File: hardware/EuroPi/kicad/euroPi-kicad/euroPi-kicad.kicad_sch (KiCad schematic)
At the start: 108 parts, among them J1 Output 1 Jack, J10 Eurorack Power 2x8 16p, J11 Conn_01x13_Socket, J12 OLED 64x128, J13 USB_B_Micro, J14 Conn_01x03_Pin, J16 Conn_02x04_Top_Bottom, J17 Conn_01x13_Pin, J18 Conn_01x04_Pin, J19 Conn_01x04_Socket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

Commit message: cleaning pcb fixing connector i2c
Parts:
- added J15: Conn_01x04_Pin, Connector_PinSocket_2.54mm:PinSocket_1x04_P2.54mm_Vertical, symbol Connector:Conn_01x04_Pin
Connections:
- net +3.3V: now also J15.2 (Pin_2)
- net CPC_SCL: now also J15.3 (Pin_3); no longer J16.1 (Pin_1), U?.2 (GP1)
- net CPC_SDA: now also J15.4 (Pin_4); no longer J16.6 (Pin_6), U?.1 (GP0)
- net GND: now also J15.1 (Pin_1)
- new net GP0: J16.6 (Pin_6), U?.1 (GP0)
- new net GP1: J16.1 (Pin_1), U?.2 (GP1)

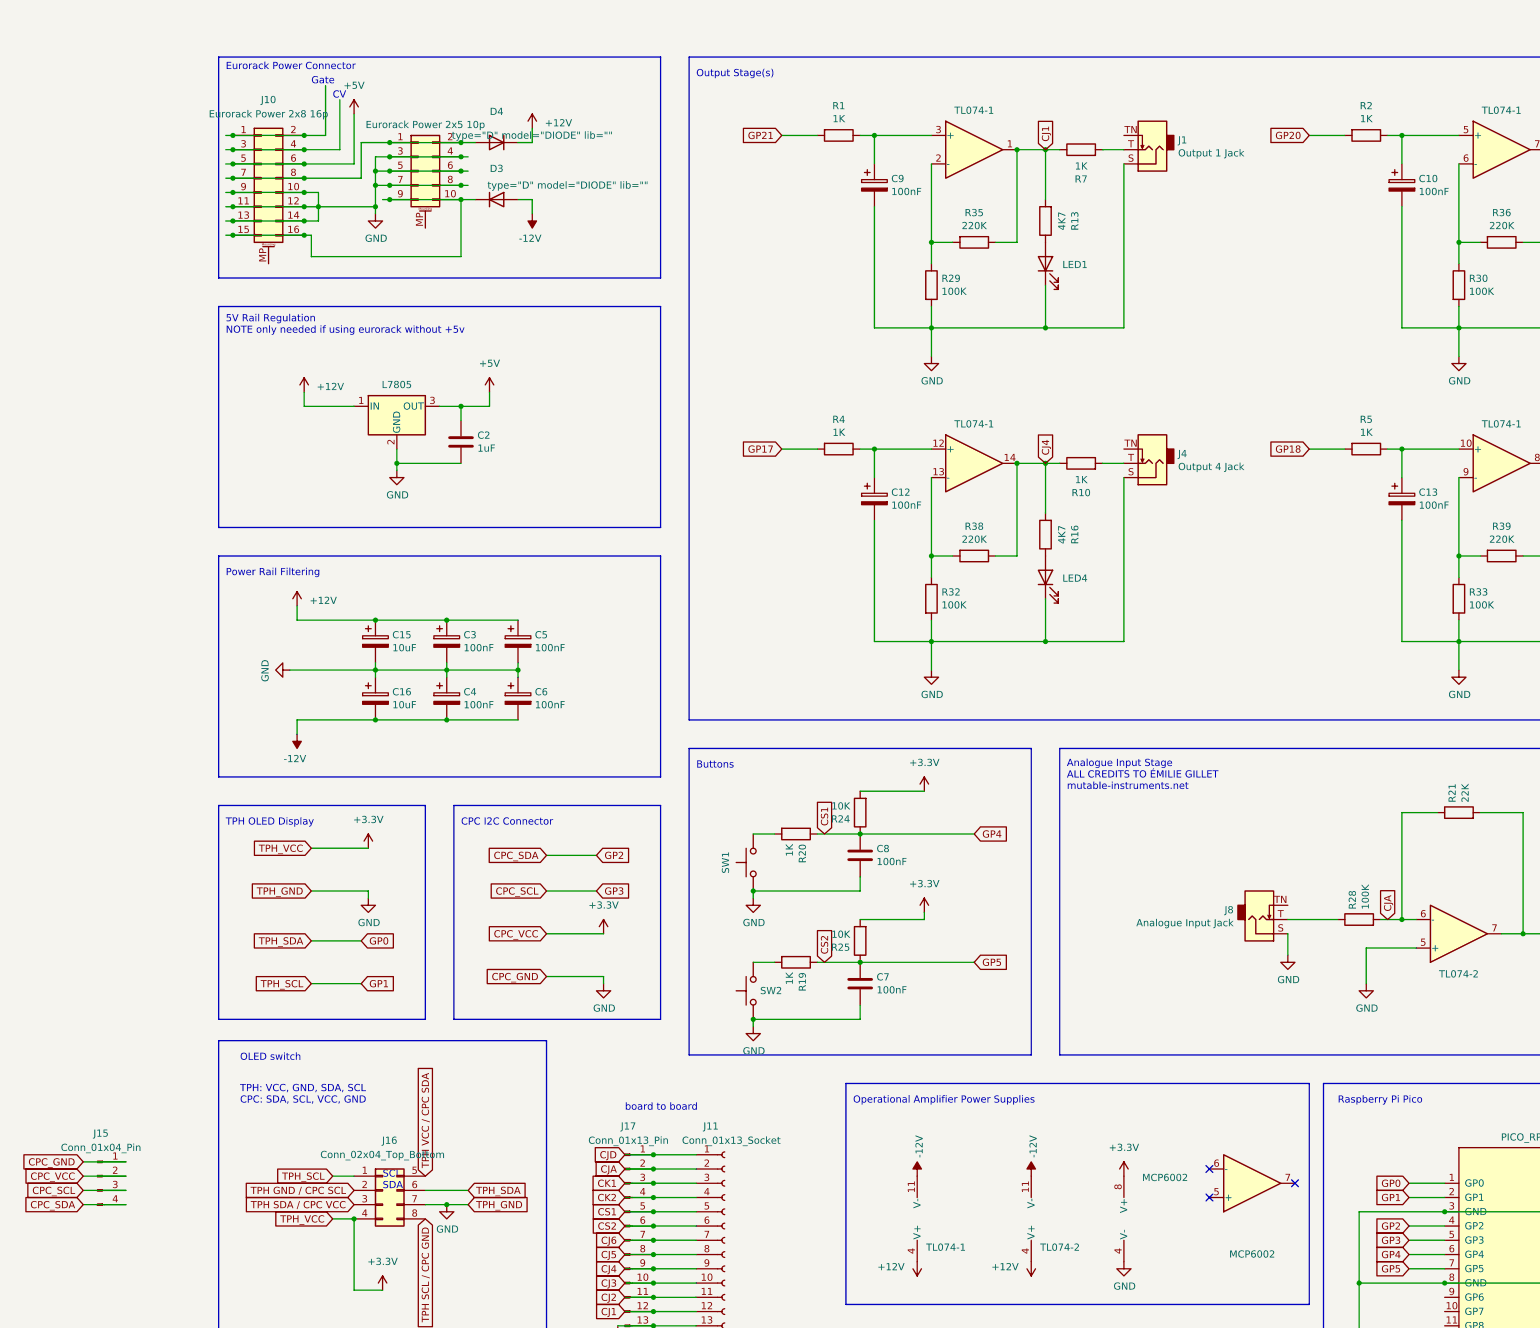
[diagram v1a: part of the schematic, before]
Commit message: fixed eurorack connector to correct pin1 imported graphics
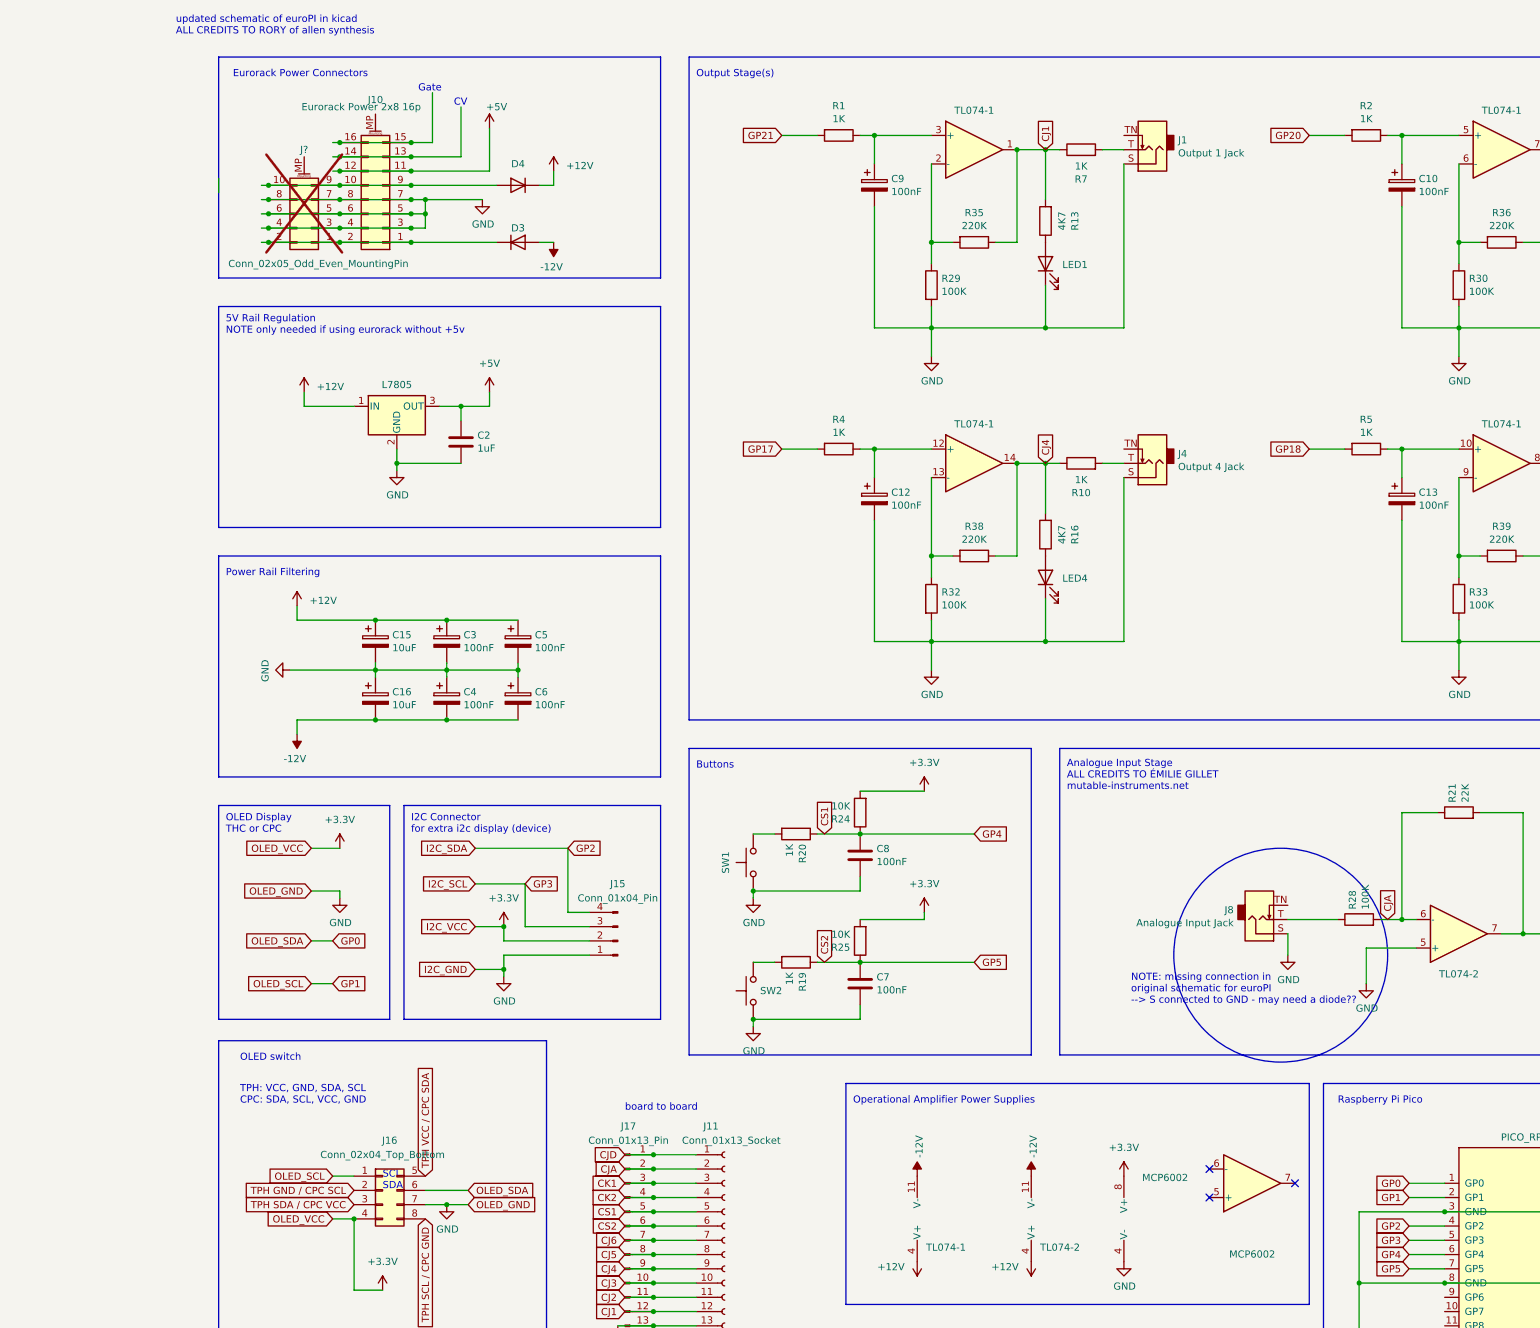
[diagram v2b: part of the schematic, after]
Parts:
- J10: footprint Connector_IDC:IDC-Header_2x08_P2.54mm_Vertical -> Library:IDC-Header_euroRack-2x08_and_2x05_P2.54mm_Vertical
- J?: value Eurorack Power 2x5 10p -> Conn_02x05_Odd_Even_MountingPin; now not fitted
- Reference? (x5): now left out of the parts list
- U?: footprint Package_TO_SOT_THT:TO-220-2_Vertical -> Package_TO_SOT_THT:TO-220-3_Vertical
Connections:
- net +5V: now also J10.11 (Pin_11), J10.12 (Pin_12); no longer J10.5 (Pin_5), J10.6 (Pin_6)
- net GND: now also J10.3 (Pin_3), J10.4 (Pin_4), J10.5 (Pin_5), J10.6 (Pin_6), J10.7 (Pin_7), J10.8 (Pin_8); no longer J10.10 (Pin_10), J10.11 (Pin_11), J10.12 (Pin_12), J10.13 (Pin_13), J10.14 (Pin_14), J10.9 (Pin_9)
- net at J10.1 (Pin_1), J10.2 (Pin_2): now also D3.2 (K), J?.1 (Pin_1), J?.2 (Pin_2)
- net CPC_SCL renamed GP3
- net CPC_SDA renamed GP2
- new net: D4.1 (A), J10.10 (Pin_10), J10.9 (Pin_9), J?.10 (Pin_10), J?.9 (Pin_9)
- new net: J10.13 (Pin_13), J10.14 (Pin_14)
- new net: J10.15 (Pin_15), J10.16 (Pin_16)
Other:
- note added: "Eurorack Power Connectors"
- note added: "I2C Connector for extra i2c display (device)"
- note added: "NOTE: missing connection in original schematic for euroPI --> S connected to GND - may need a diode??"
- note added: "OLED Display THC or CPC"
- note added: "updated schematic of euroPI in kicad ALL CREDITS TO RORY of allen synthesis"
- note removed: "CPC I2C Connector"
- note removed: "Eurorack Power Connector"
- note removed: "TPH OLED Display"
- moved on the sheet: D3, D4, J10, J15
